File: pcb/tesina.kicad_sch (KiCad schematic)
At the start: 12 parts

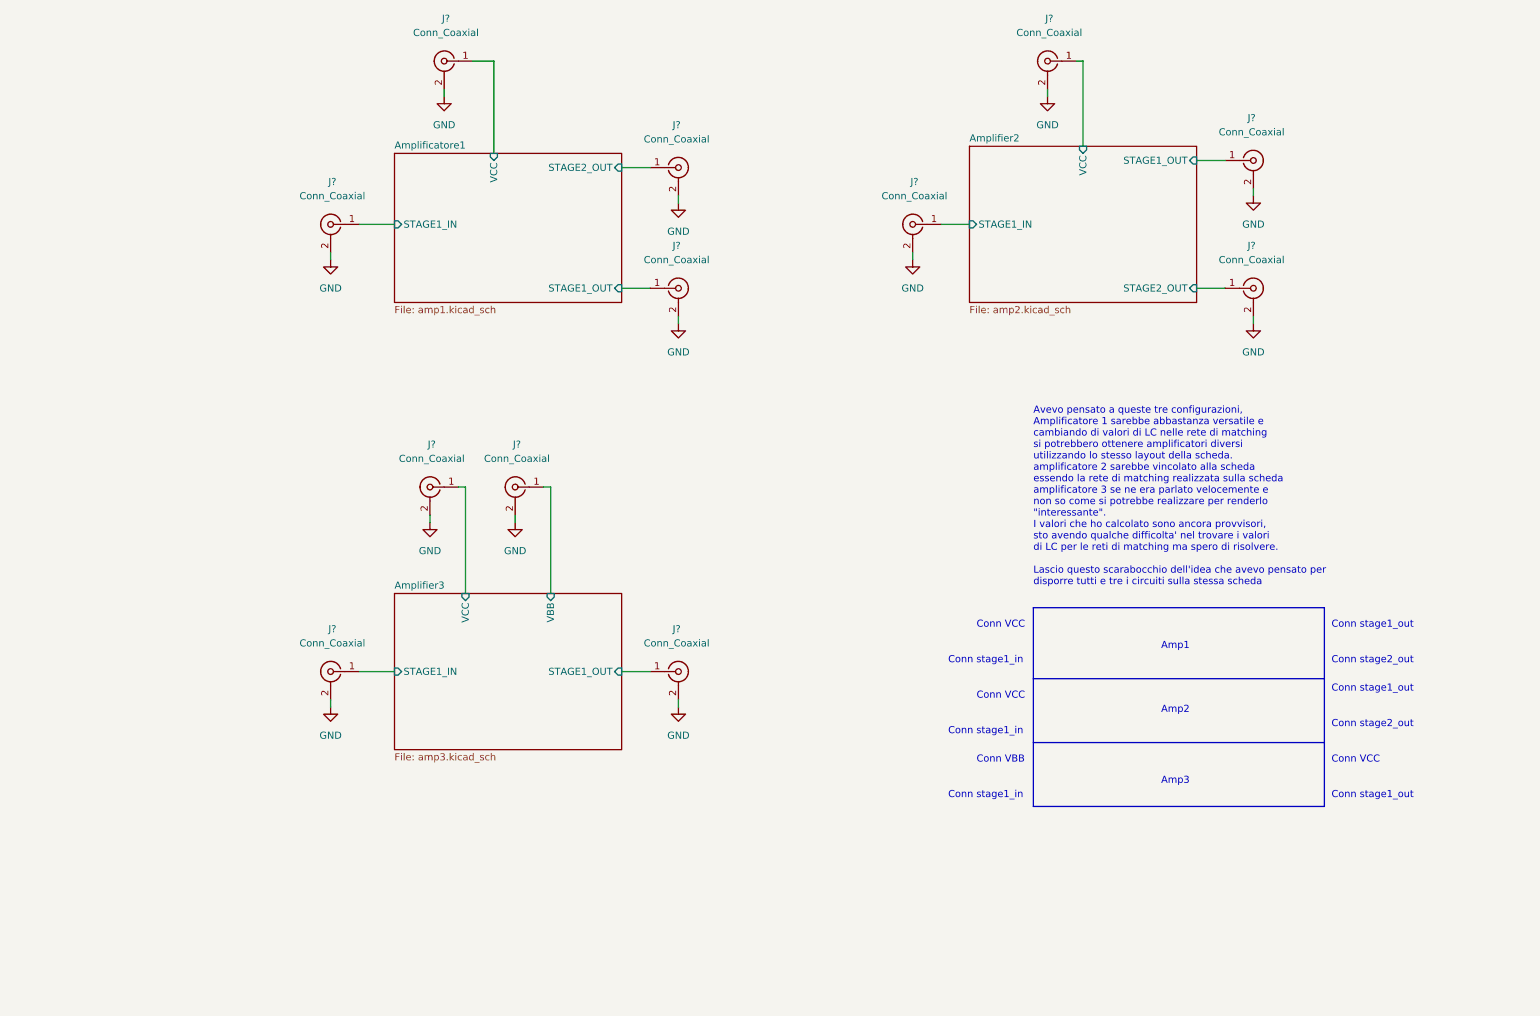
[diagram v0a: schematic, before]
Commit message: Added values for matching network
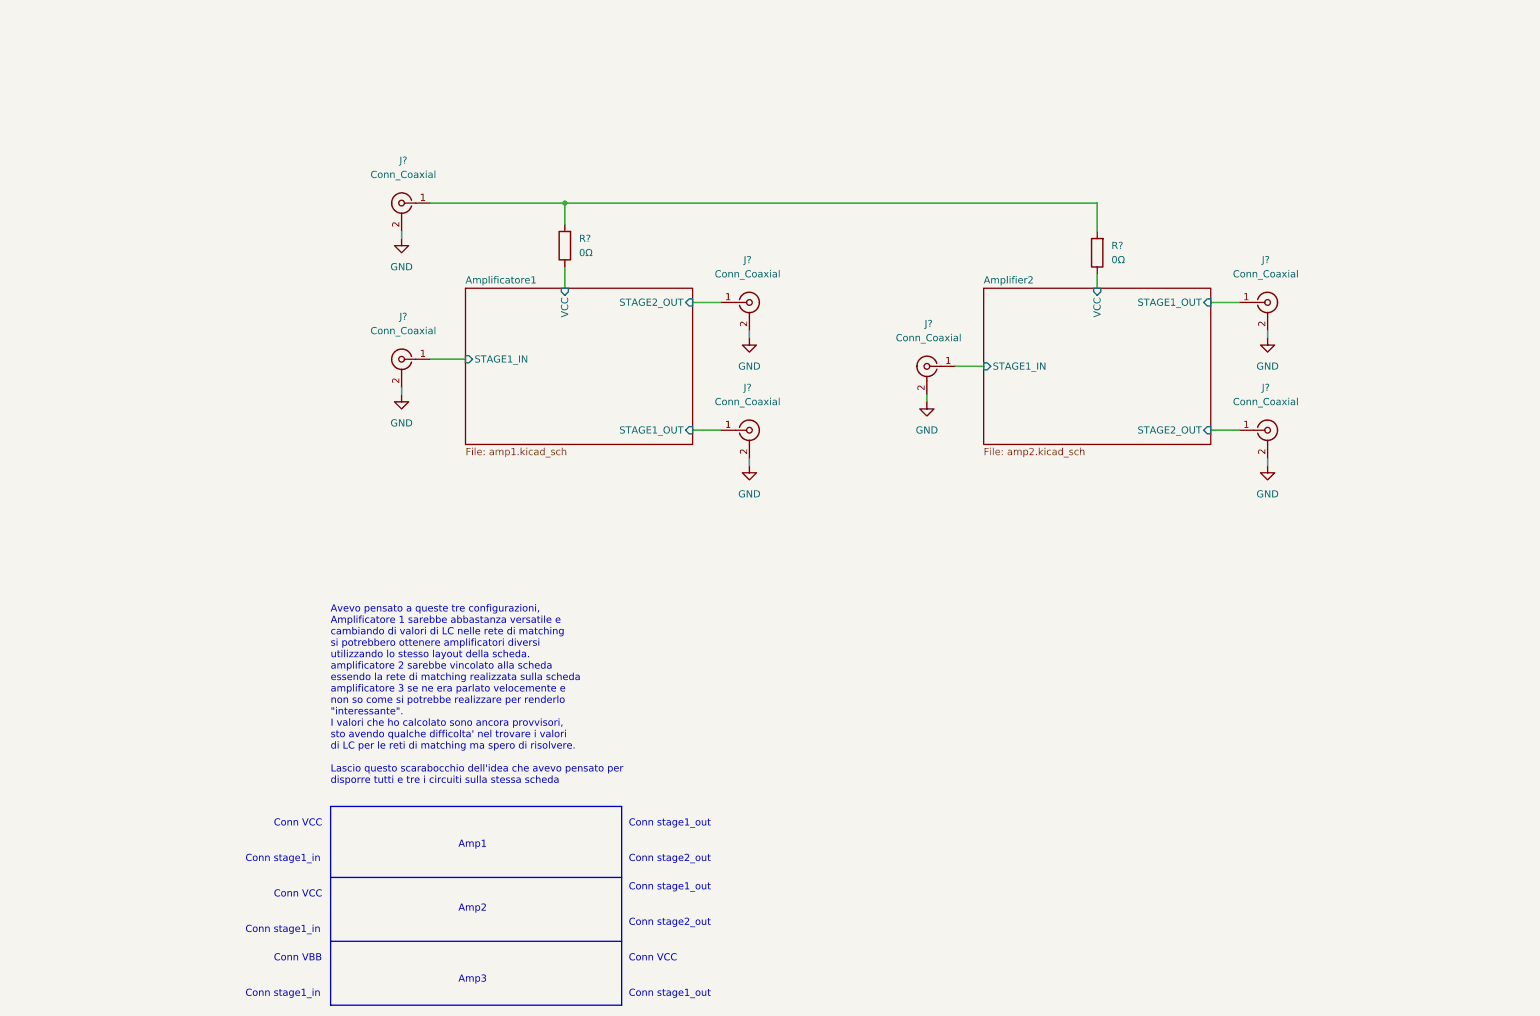
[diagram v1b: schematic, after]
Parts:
- removed J? (x5): Conn_Coaxial, Nicobigio01:Linx_CONSMA003.031-L-G, symbol Connector:Conn_Coaxial
- added R? (x2): 0Ω, symbol Device:R
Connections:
- net Amplificatore1/VCC: now also R?.1; no longer J?.1 (In)
- net Amplifier2/VCC: now also R?.1
- new net: J?.1 (In), R?.2, R?.2
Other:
- removed sheet Amplifier3
- moved on the sheet: J?

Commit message: Created LTSpice simulation and added suggested fix
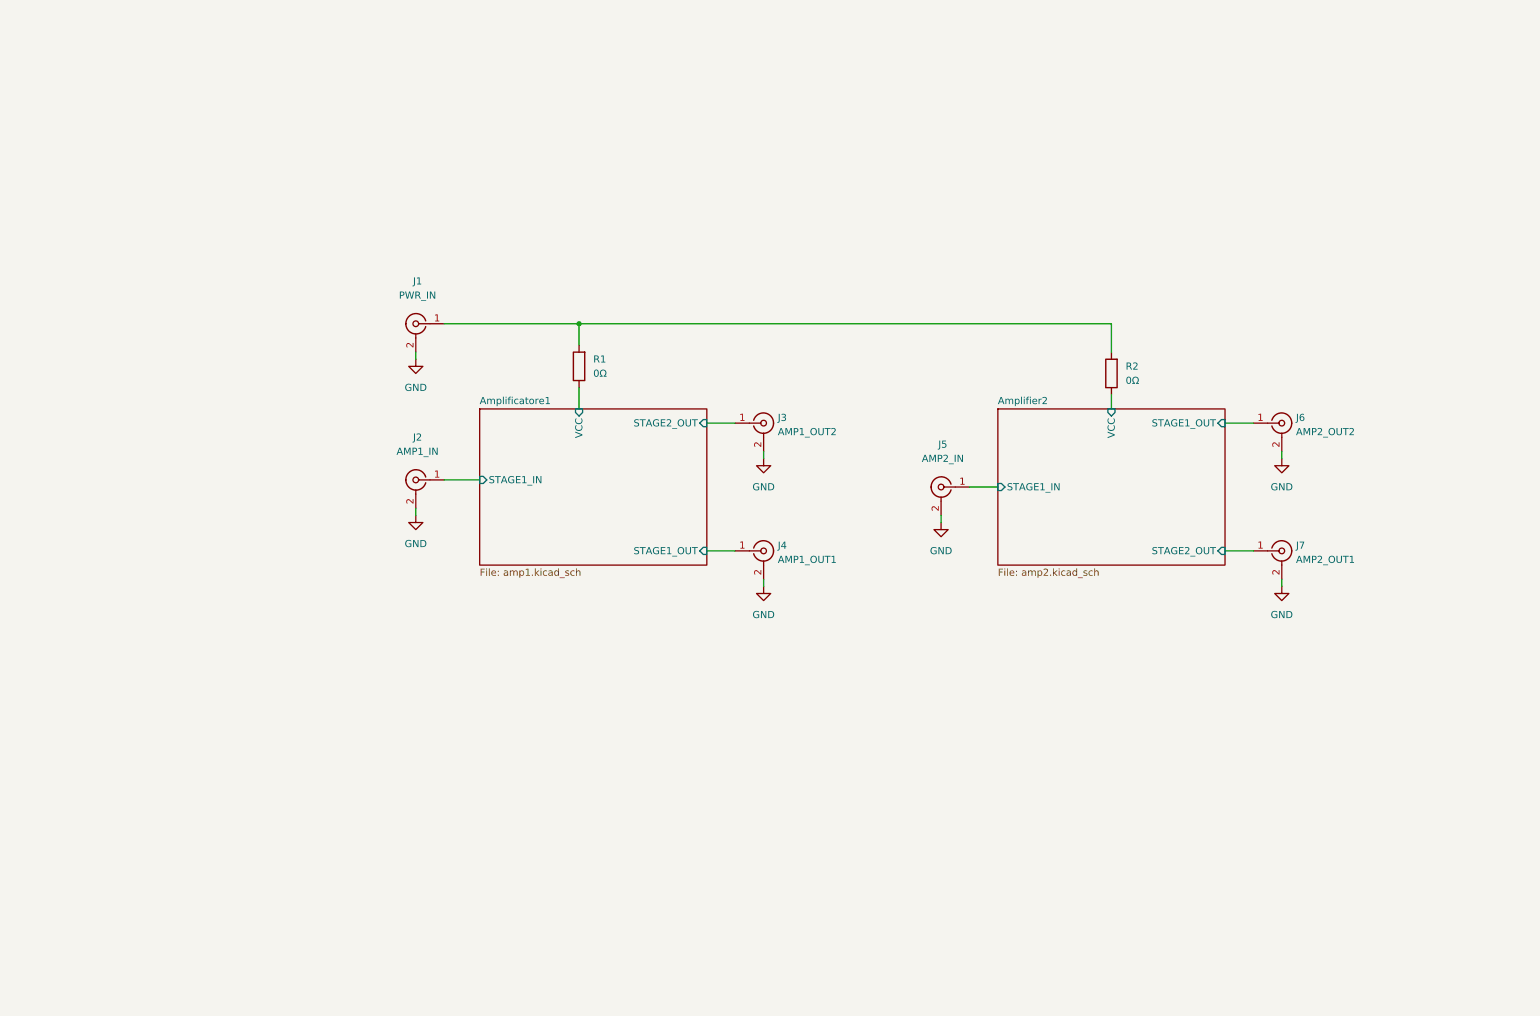
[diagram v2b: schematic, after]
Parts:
- J1: renamed from J?; value Conn_Coaxial -> PWR_IN
- J2: renamed from J?; value Conn_Coaxial -> AMP1_IN
- J3: renamed from J?; value Conn_Coaxial -> AMP1_OUT2
- J4: renamed from J?; value Conn_Coaxial -> AMP1_OUT1
- J5: renamed from J?; value Conn_Coaxial -> AMP2_IN
- J6: renamed from J?; value Conn_Coaxial -> AMP2_OUT2
- J7: renamed from J?; value Conn_Coaxial -> AMP2_OUT1
- gave numbers to parts that had none: 2
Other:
- note removed: "Amp1"
- note removed: "Amp2"
- note removed: "Amp3"
- note removed: "Avevo pensato a queste tre configurazioni, Amplificatore 1 sarebbe abbastanza versatile e cambiando di valori di LC nelle rete di matching si potrebbero ottenere amplificatori diversi utilizzando lo stesso layout della scheda. amplificatore 2 sarebbe vincolato alla scheda essendo la rete di matching realizzata sulla scheda amplificatore 3 se ne era parlato velocemente e non so come si potrebbe re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"
- note removed: "Conn VBB"
- note removed: "Conn VCC"
- note removed: "Conn stage1_in"
- note removed: "Conn stage1_out"
- note removed: "Conn stage2_out"
- moved on the sheet: J1, J2, J3, J4, J5, J6, J7, R1, R2

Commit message: Schematic modified as discussed
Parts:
- added J8: AMP3_OUT, Nicobigio01:Linx_CONSMA003.031-L-G, symbol Connector:Conn_Coaxial
- added R9: 0Ω, Resistor_SMD:R_0603_1608Metric, symbol Device:R
- J6: value AMP2_OUT2 -> AMP3_IN
- J7: value AMP2_OUT1 -> AMP2_OUT
- R1, R2: footprint (none) -> Resistor_SMD:R_0603_1608Metric
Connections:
- net GND: now also J8.2 (Ext)
- net at J1.1 (In), R1.2, R2.2: now also R9.2
- net Amplifier2/STAGE1_OUT renamed Amplifier3/STAGE1_IN
- new net Amplifier3/STAGE2_OUT: J8.1 (In)
- new net Amplifier3/VCC: R9.1
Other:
- added sheet Amplifier3 (amp2.kicad_sch)
- sheet Amplifier2 ports: added none; removed STAGE1_OUT
- moved on the sheet: J1, J2, J3, J4, J5, J7, R1, R2

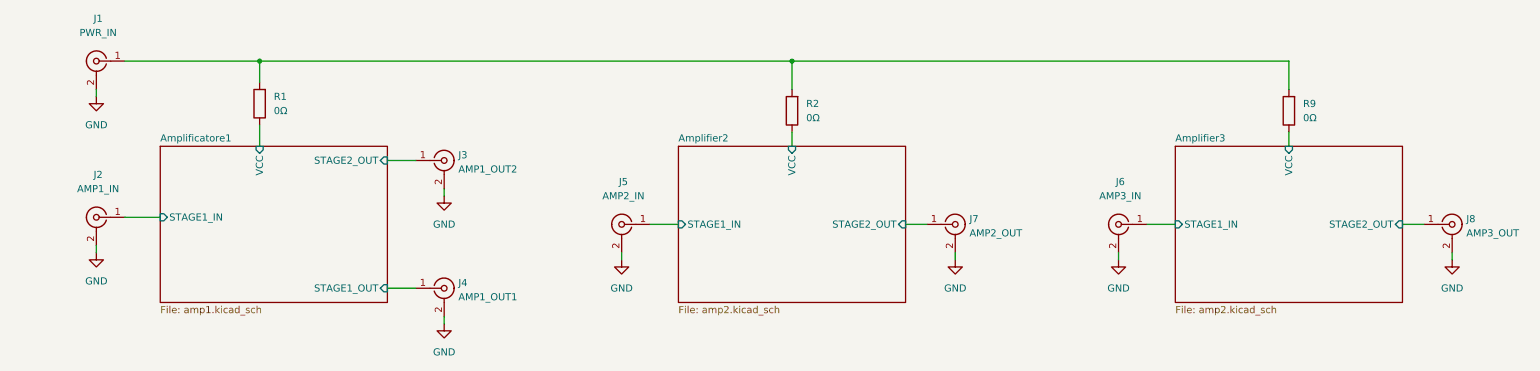
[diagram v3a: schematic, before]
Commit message: Deleted double stage, updated stub stage, L stage and PCB
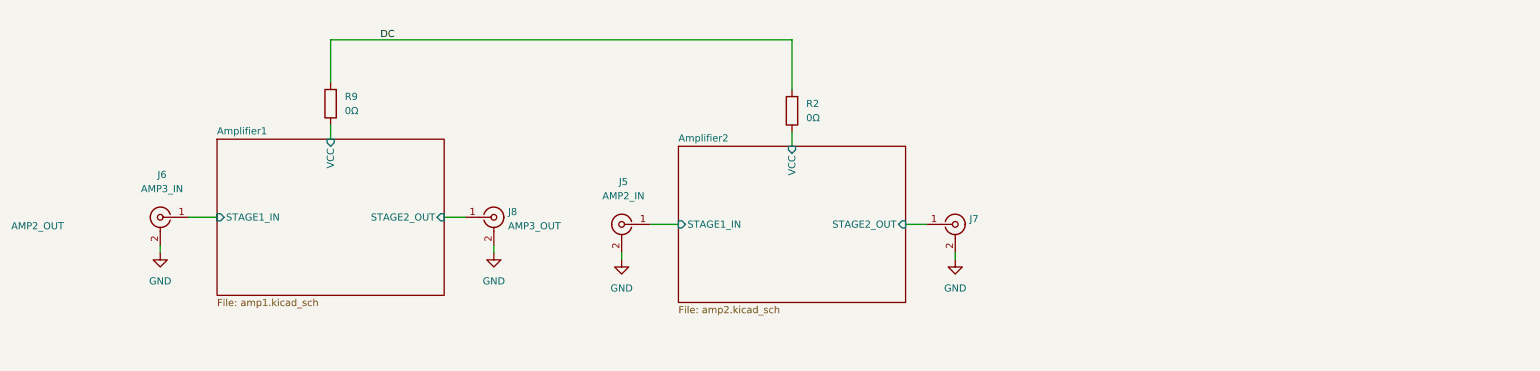
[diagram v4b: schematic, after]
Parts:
- removed J1: PWR_IN, Nicobigio01:Linx_CONSMA003.031-L-G, symbol Connector:Conn_Coaxial
- removed J2: AMP1_IN, Nicobigio01:Linx_CONSMA003.031-L-G, symbol Connector:Conn_Coaxial
- removed J3: AMP1_OUT2, Nicobigio01:Linx_CONSMA003.031-L-G, symbol Connector:Conn_Coaxial
- removed J4: AMP1_OUT1, Nicobigio01:Linx_CONSMA003.031-L-G, symbol Connector:Conn_Coaxial
- removed R1: 0Ω, Resistor_SMD:R_0603_1608Metric, symbol Device:R
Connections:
- net DC: now reaches R2.2, R9.2
- net Amplifier3/STAGE1_IN renamed Amplifier1/STAGE1_IN
- net Amplifier3/STAGE2_OUT renamed Amplifier1/STAGE2_OUT
- net Amplifier3/VCC renamed Amplifier1/VCC
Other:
- removed sheet Amplificatore1
- removed sheet Amplifier3
- added sheet Amplifier1 (amp1.kicad_sch)
- moved on the sheet: J6, J8, R9

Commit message: Started PCB Layout
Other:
- note added: "alimentazione M2 M2.5 3 viti"
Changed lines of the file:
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@@
     (stroke (width 0) (type default) (color 0 0 0 0))
+  )
+  (text "alimentazione\nM2 M2.5 3 viti" (at 81.28 49.53 0)
+    (effects (font (size 1.27 1.27)) (justify left bottom))
   )
   (label "DC" (at 69.85 68.58 0)
@@
       (effects (font (size 1.27 1.27)) hide)
     )
-    (property "Datasheet" "https://linxtechnologies.com/wp/wp-content/uploads/consma003.031-l-g-1.pdf" (id 3) (at 90.17 100.33 0)
+    (property "Datasheet" " ~" (id 3) (at 90.17 100.33 0)
       (effects (font (size 1.27 1.27)) hide)
     )
@@
       (effects (font (size 1.27 1.27)) hide)
     )
-    (property "Datasheet" "https://linxtechnologies.com/wp/wp-content/uploads/consma003.031-l-g-1.pdf" (id 3) (at 113.03 101.6 0)
+    (property "Datasheet" " ~" (id 3) (at 113.03 101.6 0)
       (effects (font (size 1.27 1.27)) hide)
     )
@@
       (effects (font (size 1.27 1.27)) hide)
     )
-    (property "Datasheet" "https://linxtechnologies.com/wp/wp-content/uploads/consma003.031-l-g-1.pdf" (id 3) (at 30.48 100.33 0)
+    (property "Datasheet" " ~" (id 3) (at 30.48 100.33 0)
       (effects (font (size 1.27 1.27)) hide)
     )
@@
       (effects (font (size 1.27 1.27)) hide)
     )
-    (property "Datasheet" "https://linxtechnologies.com/wp/wp-content/uploads/consma003.031-l-g-1.pdf" (id 3) (at 172.72 101.6 0)
+    (property "Datasheet" " ~" (id 3) (at 172.72 101.6 0)
       (effects (font (size 1.27 1.27) bold) hide)
     )

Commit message: backup version before changes
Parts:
- added H1: MountingHole_Pad, MountingHole:MountingHole_2.5mm_Pad_TopBottom, symbol Mechanical:MountingHole_Pad
- added H2, H3, H4, H5: MountingHole_Pad, MountingHole:MountingHole_2.7mm_M2.5_DIN965_Pad_TopBottom, symbol Mechanical:MountingHole_Pad
- added J1: Conn_01x02_Male, Connector_PinHeader_2.54mm:PinHeader_1x02_P2.54mm_Vertical, symbol Connector:Conn_01x02_Male
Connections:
- net DC: now also J1.1 (Pin_1)
- net GND: now also H1.1, H2.1, H3.1, H4.1, H5.1, J1.2 (Pin_2)
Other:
- moved on the sheet: J5, J6, J7, J8, R2, R9
